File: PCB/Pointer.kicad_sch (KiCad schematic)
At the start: 8 parts, among them J1 Conn_01x20, J2 Conn_01x20, J3 Conn_01x05_Pin, J4 Screw_Terminal_01x02, J5 Conn_01x03_Pin, U1 ULN2003

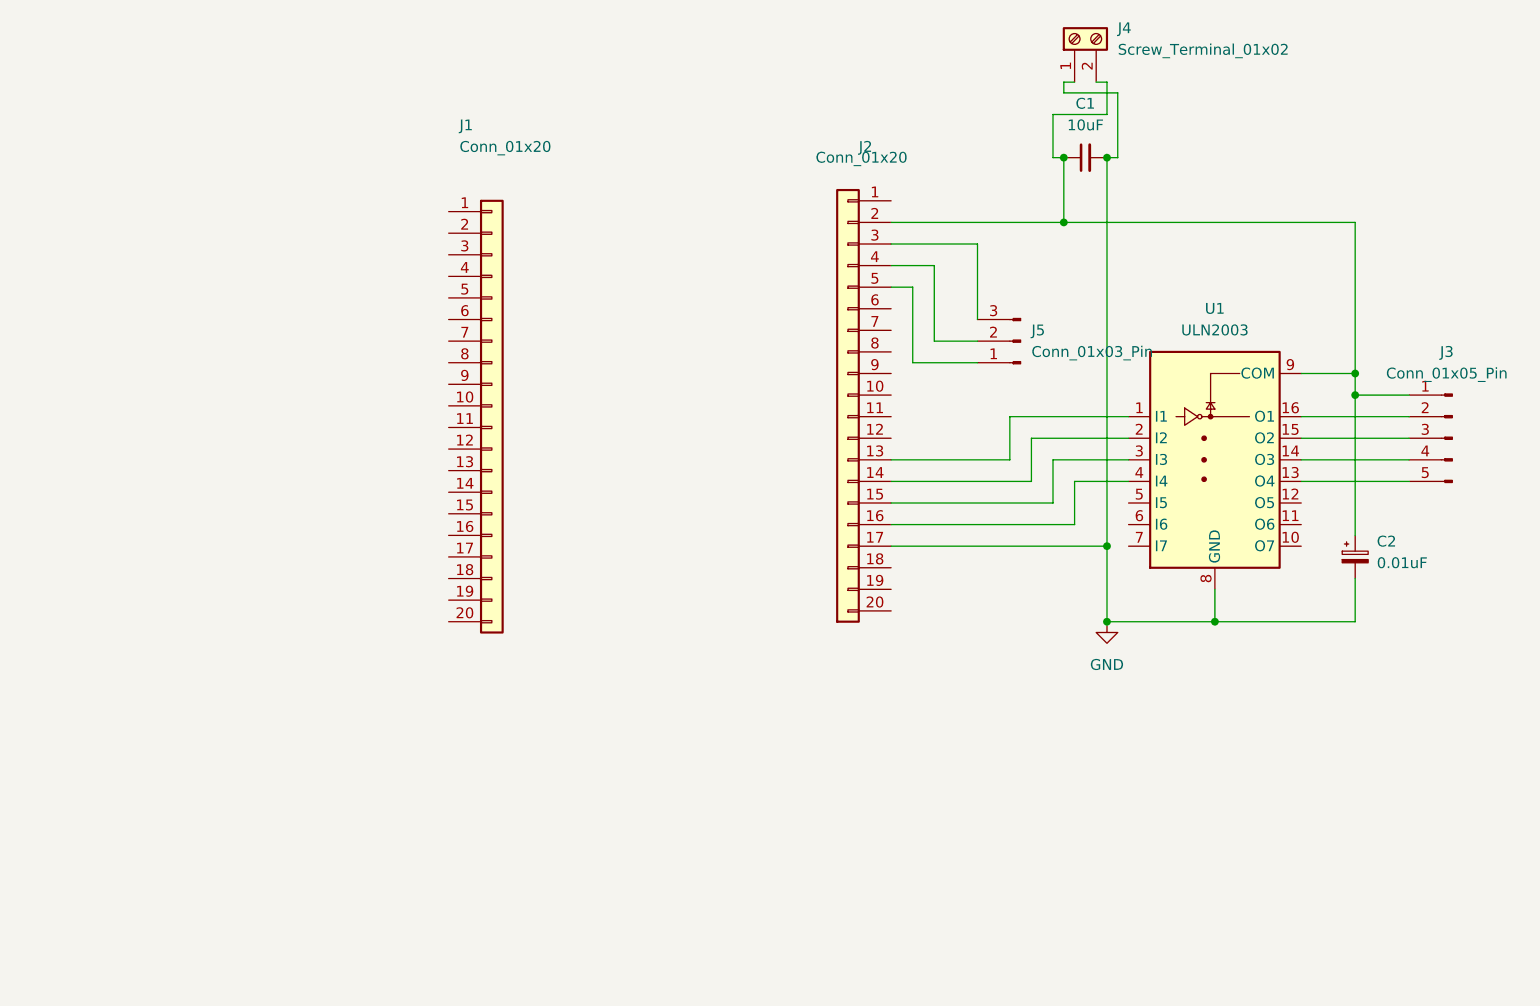
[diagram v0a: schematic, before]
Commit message: PCB Rev 1.0
Fixed MCU and servo headers
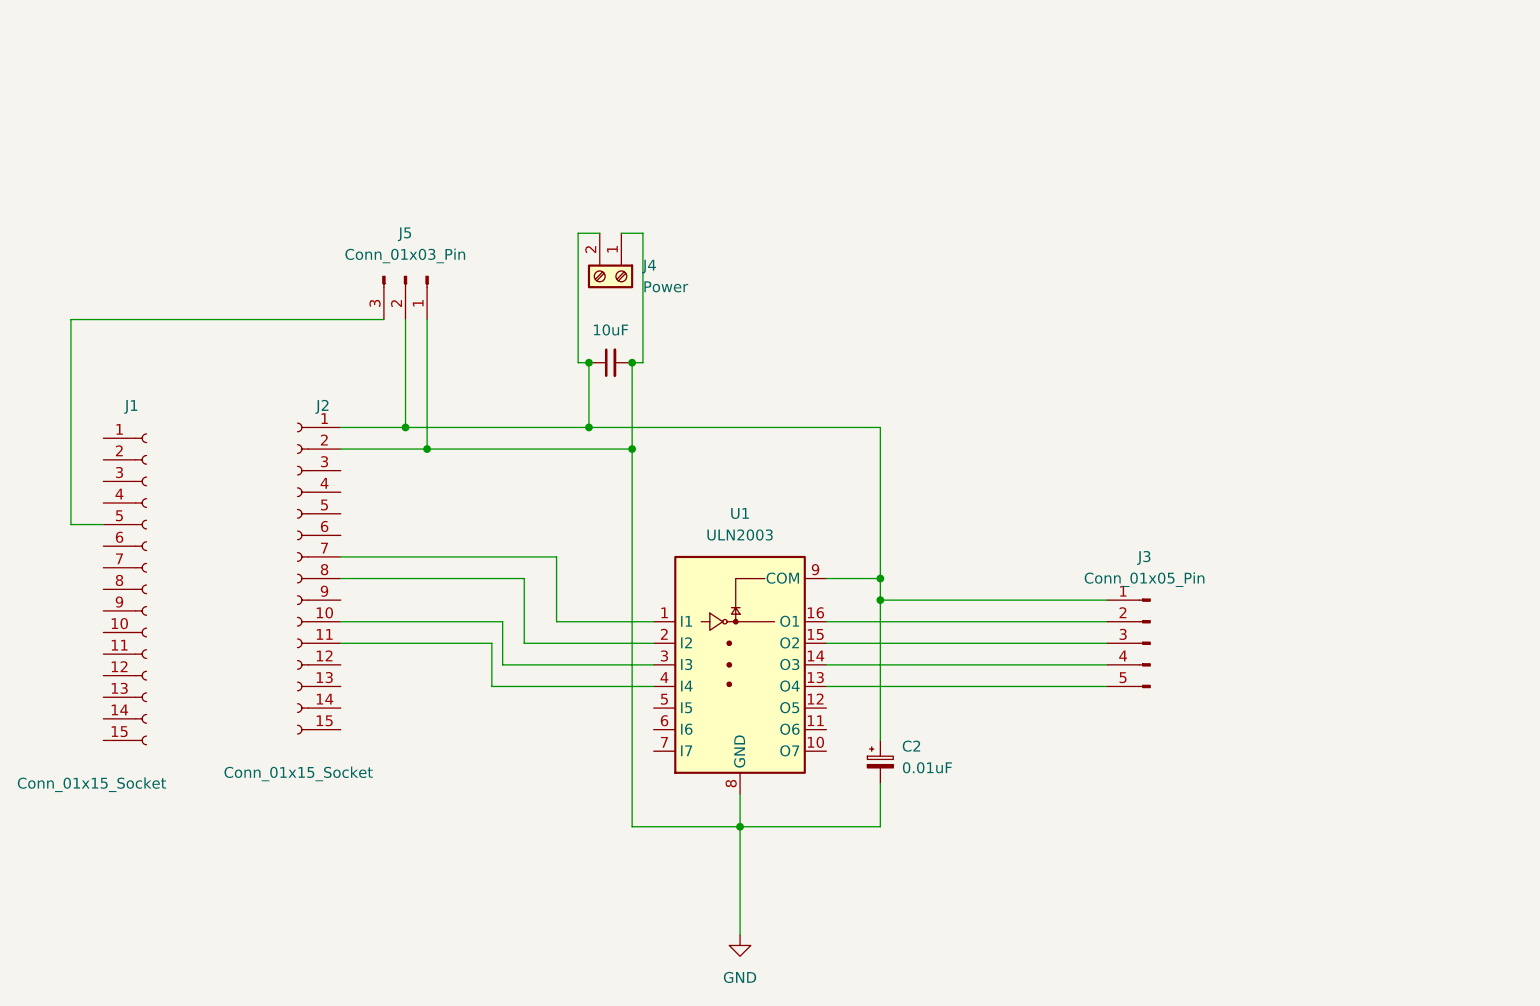
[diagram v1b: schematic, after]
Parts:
- removed J1, J2: Conn_01x20, Connector_PinSocket_2.54mm:PinSocket_1x20_P2.54mm_Vertical, symbol Connector_Generic:Conn_01x20
- added J1, J2: Conn_01x15_Socket, Connector_PinSocket_2.54mm:PinSocket_1x15_P2.54mm_Vertical, symbol Connector:Conn_01x15_Socket
- J4: value Screw_Terminal_01x02 -> Power
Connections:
- net GND: now also J5.1 (Pin_1), J2.2 (Pin_2)
- net at C1.1, C2.1, J3.1 (Pin_1)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: now also J5.2 (Pin_2), J2.1 (Pin_1)
- net at J5.3 (Pin_3): now also J1.5 (Pin_5)
- net at U1.1 (I1): now also J2.7 (Pin_7)
- net at U1.2 (I2): now also J2.8 (Pin_8)
- net at U1.3 (I3): now also J2.10 (Pin_10)
- net at U1.4 (I4): now also J2.11 (Pin_11)
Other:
- moved on the sheet: C2, J3, J4, J5, U1
